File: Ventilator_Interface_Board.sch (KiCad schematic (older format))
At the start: 51 parts, among them J1 ROTARY CONTROLS, J3 ALARM, J4 LCD DISPLAY, J5 OPTICAL SWITCH, J6 HOME LIMIT SWITCH, P1 Power, P2 Analog, P3 Digital, P4 Digital, P5 CONN_01X01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

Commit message: Rev A - pre-release
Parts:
- removed J3: ALARM, Ventilator:Molex_KK-254_1x04_P2.54mm_Horizontal, symbol Connector_Generic:Conn_01x04
- removed J4: LCD DISPLAY, Ventilator:Molex_KK-254_1x12_P2.54mm_Horizontal, symbol Connector_Generic:Conn_01x12
- removed J5: OPTICAL SWITCH, Ventilator:Molex_KK-254_1x05_P2.54mm_Horizontal, symbol Connector_Generic:Conn_01x05
- removed J6: HOME LIMIT SWITCH, Ventilator:Molex_KK-254_1x06_P2.54mm_Horizontal, symbol Connector_Generic:Conn_01x06
- removed U1: HSCMRRN100MDAA5, Ventilator:SMT-8W_7.5x8.8mm_P2.54mm, symbol Ventilator:HSCMRRN100MDAA5
- removed U2: HSCDRRN100MDAA5, Ventilator:DIP-8_W13.08mm, symbol Ventilator:HSCMRRN100MDAA5
- added C7: 1uF, Capacitor_SMD:C_0603_1608Metric, symbol Device:C
- added C8: 470pF, Capacitor_SMD:C_0603_1608Metric, symbol Device:C
- added J2, J3, J4: Conn_01x08, Ventilator:PhoenixContact_PTSA_1,5_8-3_5-Z_1x08_P3.50mm_Vertical, symbol Connector_Generic:Conn_01x08
- added R10: 330R, Resistor_SMD:R_0603_1608Metric, symbol Device:R
- added R9: 10K, Resistor_SMD:R_0603_1608Metric, symbol Device:R
- added U1: MP3V5004GP, Ventilator:SOP_16.8x7.62mm_P2.54mm, symbol Ventilator:MP3V5004GP
- J1: value ROTARY CONTROLS -> Conn_01x08; footprint Ventilator:Molex_KK-254_1x08_P2.54mm_Horizontal -> Ventilator:PhoenixContact_PTSA_1,5_8-3_5-Z_1x08_P3.50mm_Vertical
- R3: value 10K -> DNF
- R7: value 330R -> 0R
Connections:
- net +3V3: now also R7.2
- net +5V: now also J1.2 (Pin_2), J1.3 (Pin_3), R2.2, R3.2, R4.2, R5.2, J3.2 (Pin_2), J3.7 (Pin_7), J4.4 (Pin_4), R9.2; no longer C4.2, J1.1 (Pin_1), R2.1, R3.1, R4.1, R5.1
- net BPM: now also J3.4 (Pin_4); no longer J1.3 (Pin_3)
- net BUZZER_LED: now also J2.5 (Pin_5), J2.7 (Pin_7)
- net GND: now also J1.1 (Pin_1), J1.5 (Pin_5), C7.1, C8.1, J2.4 (Pin_4), J2.6 (Pin_6), J3.8 (Pin_8), J4.1 (Pin_1), J4.6 (Pin_6), R10.2, U1.3 (GND); no longer J1.6 (Pin_6), R7.2
- net HOME_LIMIT_SW: now also J4.8 (Pin_8), R9.1; no longer R3.2
- net IF_RATE: now also J3.5 (Pin_5); no longer J1.4 (Pin_4)
- net LCD_D4: now also J1.7 (Pin_7)
- net LCD_D5: now also J1.8 (Pin_8)
- net LCD_D6: now also J2.1 (Pin_1)
- net LCD_D7: now also J2.2 (Pin_2)
- net LCD_EN: now also J1.6 (Pin_6)
- net LCD_RS: now also J1.4 (Pin_4)
- net MAX_PRESSURE: now also J3.6 (Pin_6); no longer J1.5 (Pin_5)
- net OPTICAL_SW: now also R2.1, J4.3 (Pin_3); no longer R2.2
- net PRESSURE_SENSOR: now also C8.2, U1.4 (VOUT)
- net TIDAL_VOLUME: now also J3.3 (Pin_3); no longer J1.2 (Pin_2)
- net at R6.1: now also J2.3 (Pin_3)
- net at R7.1: now also C4.2, R3.1, C7.2, U1.2 (VDD)
- net at R8.1: now also J4.5 (Pin_5)
- net at R1.1: now also J2.8 (Pin_8)
- new net: J4.7 (Pin_7), R5.1
- new net: J4.2 (Pin_2), R4.1
- new net: J3.1 (Pin_1), R10.1
- no-connect marks 25 -> 17
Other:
- note added: "5V/3.3V POWER OPTION\nMP3V5004G Series = 3.3V"
- note added: "ALARMS"
- note added: "CONTROLS"
- note added: "HOME SW"
- note added: "LCD"
- note added: "OPTICAL SW"
- note removed: "(4 x P160KNP-0EC15B10K)"
- note removed: "(JHD659)"
- note removed: "(OPB911W55Z)"
- note removed: "(PT-2038WQ)"
- note removed: "DUAL FOOTPRINT\nSM & DIP OPTIONS"
- note removed: "PIN 1: BUZZER+\nPIN 2: BUZZER-\nPIN 3: LED_A\nPIN 4: LED_K"
- moved on the sheet: C4, R1, R2, R4, R5, R6, R8

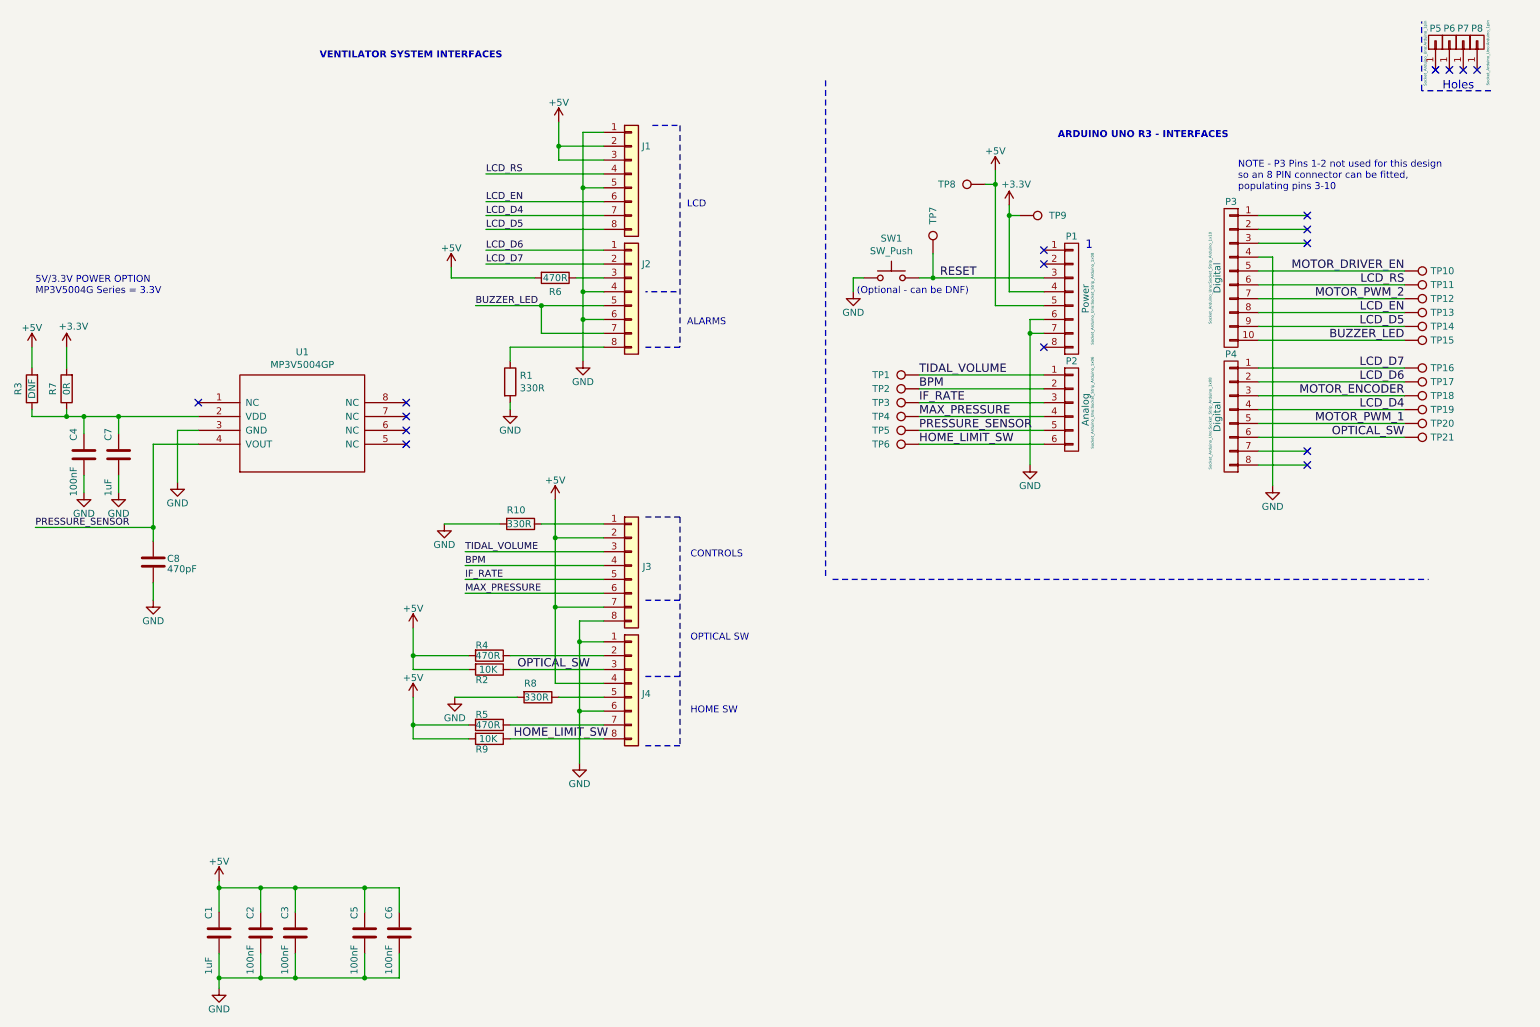
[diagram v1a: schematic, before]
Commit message: minor changes to make design more flexible
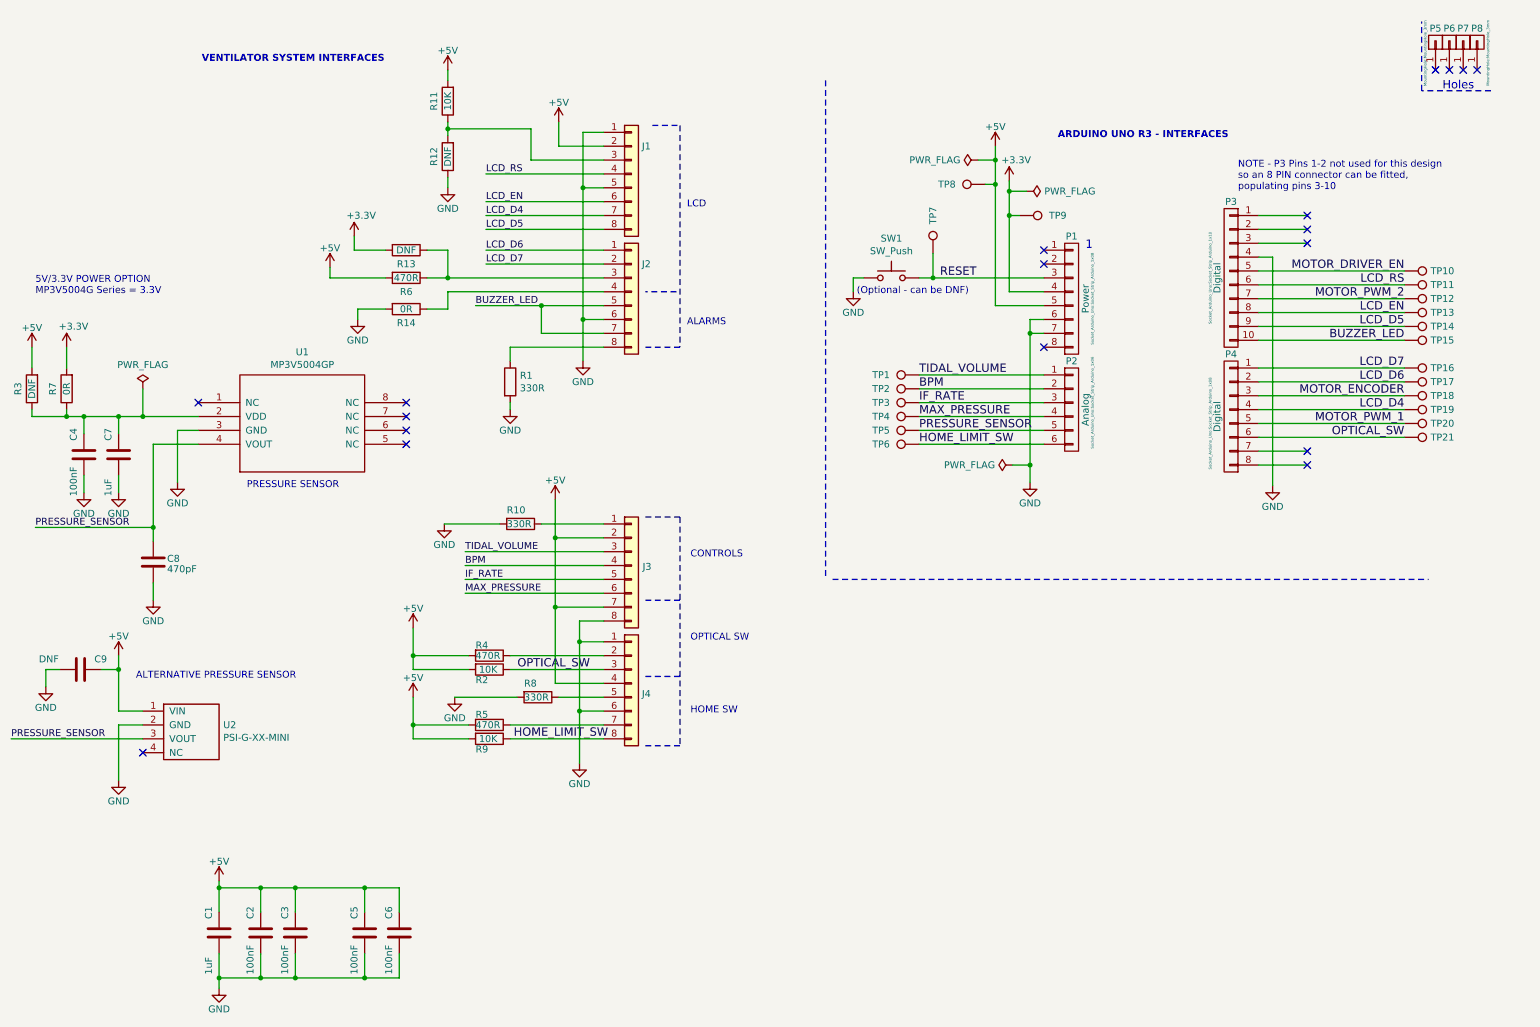
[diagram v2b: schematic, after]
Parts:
- added C9: DNF, Capacitor_SMD:C_0603_1608Metric, symbol Device:C
- added R11: 10K, Resistor_SMD:R_0603_1608Metric, symbol Device:R
- added R12, R13: DNF, Resistor_SMD:R_0603_1608Metric, symbol Device:R
- added R14: 0R, Resistor_SMD:R_0603_1608Metric, symbol Device:R
- added U2: PSI-G-XX-MINI, Connector_PinHeader_2.54mm:PinHeader_1x04_P2.54mm_Vertical, symbol Ventilator:PSI-G-XX-MINI
- P5, P6, P7, P8: footprint Socket_Arduino_Uno:Arduino_1pin -> MountingHole:MountingHole_3mm
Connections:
- net +3V3: now also R13.2
- net +5V: now also C9.2, R11.2, U2.1 (VIN); no longer J1.3 (Pin_3)
- net GND: now also C9.1, R12.1, R14.2, U2.2 (GND); no longer J2.4 (Pin_4)
- net PRESSURE_SENSOR: now also U2.3 (VOUT)
- net at J2.3 (Pin_3), R6.1: now also R13.1
- new net: J1.3 (Pin_3), R11.1, R12.2
- new net: J2.4 (Pin_4), R14.1
- no-connect marks 17 -> 18
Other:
- note added: "ALTERNATIVE PRESSURE SENSOR"
- note added: "PRESSURE SENSOR"
- moved on the sheet: R6
